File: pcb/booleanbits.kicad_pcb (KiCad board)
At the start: 2 copper layers, 34.3 x 17.8 mm, 3 parts, among them J1 Conn_01x04, J2 Conn_01x04, U1 SN74LVC1G08DBVR

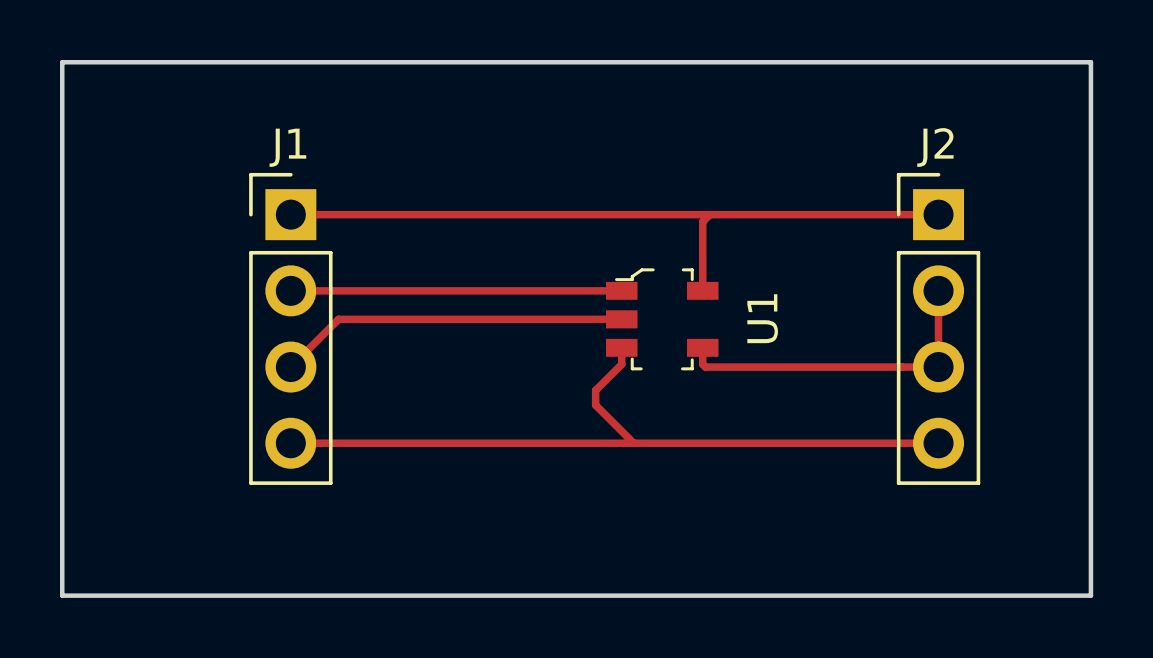
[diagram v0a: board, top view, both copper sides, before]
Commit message: Adding version with better edge footprint. Need bigger traces for my CNC
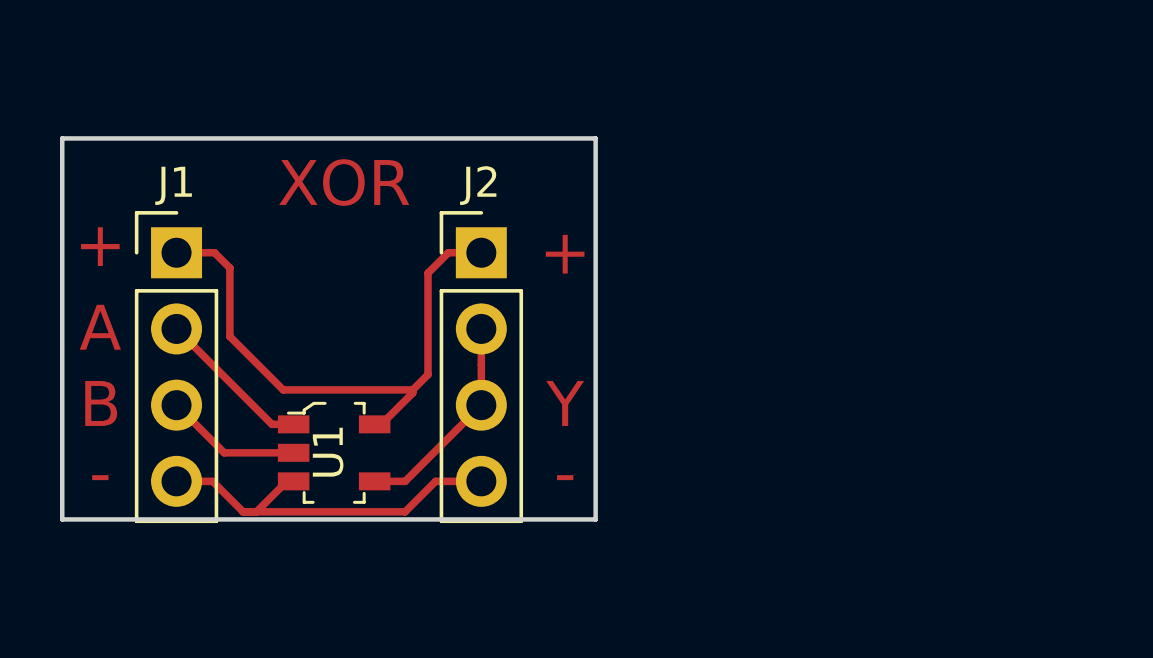
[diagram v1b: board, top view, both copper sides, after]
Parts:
- moved J2 15.3 mm to (35.6, 22.9)
- moved U1 11.8 mm to (30.7, 29.5)
- moved J1 4.02 mm to (25.4, 22.9)
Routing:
- net Net-(J1-Pad4): track 25.7 -> 13.1 mm
- net Net-(J1-Pad3): track 11.7 -> 4.56 mm
- net Net-(J1-Pad2): track 11.0 -> 5.22 mm
- net Net-(J1-Pad1): track 24.2 -> 19.1 mm
- net Net-(J2-Pad2): track 11.0 -> 7.15 mm
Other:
- board size 34.3 x 17.8 mm -> 17.8 x 12.7 mm
- board text added: "+"
- board text added: "-"
- board text added: "A"
- board text added: "B"
- board text added: "XOR"
- board text added: "Y"
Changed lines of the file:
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@@
   (general
     (links 8)
-    (no_connects 8)
-    (area 21.514999 16.434999 55.955001 34.365001)
+    (no_connects 0)
+    (area 20.652381 18.974999 40.30762 37.222857)
     (thickness 1.6)
-    (drawings 4)
-    (tracks 18)
+    (drawings 12)
+    (tracks 28)
     (zones 0)
     (modules 3)
@@
     (pad_to_mask_clearance 0.2)
     (aux_axis_origin 0 0)
-    (visible_elements FFFFEF7F)
+    (grid_origin 21.59 31.75)
+    (visible_elements FFFFFF7F)
     (pcbplotparams
-      (layerselection 0x00030_80000001)
+      (layerselection 0x01080_00000001)
       (usegerberextensions false)
       (excludeedgelayer true)
@@
       (viasonmask false)
       (mode 1)
-      (useauxorigin false)
+      (useauxorigin true)
       (hpglpennumber 1)
       (hpglpenspeed 20)
@@
       (psa4output false)
       (plotreference true)
-      (plotvalue true)
+      (plotvalue false)
       (plotinvisibletext false)
       (padsonsilk false)
@@
       (outputformat 1)
       (mirror false)
-      (drillshape 1)
+      (drillshape 0)
       (scaleselection 1)
-      (outputdirectory /tmp/foo.svg))
+      (outputdirectory plot/))
   )
   (net 0 "")
@@
   )
   (module digikey-footprints:SOT-753 (layer F.Cu)
-    (at 41.59 25.08 270)
-    (fp_text reference U1 (at -0.025 -3.375 270) (layer F.SilkS)
+    (at 30.654 29.53 270)
+    (fp_text reference U1 (at -0.025 0.174 270) (layer F.SilkS)
       (effects (font (size 1 1) (thickness 0.15)))
     )
@@
   )
   (module Pin_Headers:Pin_Header_Straight_1x04_Pitch2.54mm (layer F.Cu)
-    (at 29.21 21.59)
+    (at 25.4 22.86)
     (descr "Through hole straight pin header, 1x04, 2.54mm pitch, single row")
     (tags "Through hole pin header THT 1x04 2.54mm single row")
@@
   )
   (module Pin_Headers:Pin_Header_Straight_1x04_Pitch2.54mm (layer F.Cu)
-    (at 50.8 21.59)
+    (at 35.56 22.86)
     (descr "Through hole straight pin header, 1x04, 2.54mm pitch, single row")
     (tags "Through hole pin header THT 1x04 2.54mm single row")
@@
     )
   )
-  (gr_line (start 55.88 34.29) (end 21.59 34.29) (layer Edge.Cuts) (width 0.15))
-  (gr_line (start 55.88 16.51) (end 55.88 34.29) (layer Edge.Cuts) (width 0.15))
-  (gr_line (start 21.59 16.51) (end 55.88 16.51) (layer Edge.Cuts) (width 0.15))
-  (gr_line (start 21.59 34.29) (end 21.59 16.51) (layer Edge.Cuts) (width 0.15))
-  (segment (start 43.18 21.59) (end 50.8 21.59) (width 0.25) (layer F.Cu) (net 1))
-  (segment (start 29.21 21.59) (end 43.18 21.59) (width 0.25) (layer F.Cu) (net 1))
-  (segment (start 43.18 21.59) (end 42.94 21.83) (width 0.25) (layer F.Cu) (net 1))
-  (segment (start 42.94 21.83) (end 42.94 24.13) (width 0.25) (layer F.Cu) (net 1))
-  (segment (start 50.8 24.13) (end 50.8 26.67) (width 0.25) (layer F.Cu) (net 2))
-  (segment (start 42.94 26.03) (end 42.94 26.58) (width 0.25) (layer F.Cu) (net 2))
-  (segment (start 42.94 26.58) (end 43.03 26.67) (width 0.25) (layer F.Cu) (net 2))
-  (segment (start 43.03 26.67) (end 49.597919 26.67) (width 0.25) (layer F.Cu) (net 2))
-  (segment (start 49.597919 26.67) (end 50.8 26.67) (width 0.25) (layer F.Cu) (net 2))
-  (segment (start 50.8 29.21) (end 40.64 29.21) (width 0.25) (layer F.Cu) (net 3))
-  (segment (start 40.64 29.21) (end 29.21 29.21) (width 0.25) (layer F.Cu) (net 3))
-  (segment (start 39.37 27.45) (end 39.37 27.94) (width 0.25) (layer F.Cu) (net 3))
-  (segment (start 39.37 27.94) (end 40.64 29.21) (width 0.25) (layer F.Cu) (net 3))
-  (segment (start 40.24 26.03) (end 40.24 26.58) (width 0.25) (layer F.Cu) (net 3))
-  (segment (start 40.24 26.58) (end 39.37 27.45) (width 0.25) (layer F.Cu) (net 3))
-  (segment (start 40.24 25.08) (end 30.8 25.08) (width 0.25) (layer F.Cu) (net 4))
-  (segment (start 30.8 25.08) (end 29.21 26.67) (width 0.25) (layer F.Cu) (net 4))
-  (segment (start 29.21 24.13) (end 40.24 24.13) (width 0.25) (layer F.Cu) (net 5))
+  (gr_text XOR (at 30.988 20.574) (layer F.Cu)
+    (effects (font (size 1.5 1.5) (thickness 0.3)))
+  )
+  (gr_text - (at 38.354 30.226) (layer F.Cu)
+    (effects (font (size 1.5 1.5) (thickness 0.3)))
+  )
+  (gr_text + (at 38.354 22.86) (layer F.Cu)
+    (effects (font (size 1.5 1.5) (thickness 0.3)))
+  )
+  (gr_text Y (at 38.354 27.94) (layer F.Cu)
+    (effects (font (size 1.5 1.5) (thickness 0.3)))
+  )
+  (gr_text + (at 22.86 22.606) (layer F.Cu)
+    (effects (font (size 1.5 1.5) (thickness 0.3)))
+  )
+  (gr_text - (at 22.86 30.226) (layer F.Cu)
+    (effects (font (size 1.5 1.5) (thickness 0.3)))
+  )
+  (gr_text B (at 22.86 27.94) (layer F.Cu)
+    (effects (font (size 1.5 1.5) (thickness 0.3)))
+  )
+  (gr_text A (at 22.86 25.4) (layer F.Cu)
+    (effects (font (size 1.5 1.5) (thickness 0.3)))
+  )
+  (gr_line (start 39.37 19.05) (end 21.59 19.05) (layer Edge.Cuts) (width 0.15))
+  (gr_line (start 39.37 31.75) (end 39.37 19.05) (layer Edge.Cuts) (width 0.15))
+  (gr_line (start 21.59 31.75) (end 39.37 31.75) (layer Edge.Cuts) (width 0.15))
+  (gr_line (start 21.59 19.05) (end 21.59 31.75) (layer Edge.Cuts) (width 0.15))
+  (segment (start 25.4 22.86) (end 26.67 22.86) (width 0.25) (layer F.Cu) (net 1))
+  (segment (start 26.67 22.86) (end 27.178 23.368) (width 0.25) (layer F.Cu) (net 1))
+  (segment (start 27.178 23.368) (end 27.178 25.654) (width 0.25) (layer F.Cu) (net 1))
+  (segment (start 27.178 25.654) (end 28.956 27.432) (width 0.25) (layer F.Cu) (net 1))
+  (segment (start 28.956 27.432) (end 33.274 27.432) (width 0.25) (layer F.Cu) (net 1))
+  (segment (start 33.274 27.432) (end 33.274 27.535) (width 0.25) (layer F.Cu) (net 1))
+  (segment (start 33.274 27.535) (end 32.229 28.58) (width 0.25) (layer F.Cu) (net 1))
+  (segment (start 32.229 28.58) (end 32.004 28.58) (width 0.25) (layer F.Cu) (net 1))
+  (segment (start 33.782 23.538) (end 34.46 22.86) (width 0.25) (layer F.Cu) (net 1))
+  (segment (start 33.782 26.924) (end 33.782 23.538) (width 0.25) (layer F.Cu) (net 1))
+  (segment (start 33.274 27.432) (end 33.782 26.924) (width 0.25) (layer F.Cu) (net 1))
+  (segment (start 34.46 22.86) (end 35.56 22.86) (width 0.25) (layer F.Cu) (net 1))
+  (segment (start 35.56 25.4) (end 35.56 26.602081) (width 0.25) (layer F.Cu) (net 2))
+  (segment (start 35.56 26.602081) (end 35.56 27.94) (width 0.25) (layer F.Cu) (net 2))
+  (segment (start 32.004 30.48) (end 33.02 30.48) (width 0.25) (layer F.Cu) (net 2))
+  (segment (start 33.02 30.48) (end 35.56 27.94) (width 0.25) (layer F.Cu) (net 2))
+  (segment (start 27.618081 31.496) (end 28.063 31.496) (width 0.25) (layer F.Cu) (net 3))
+  (segment (start 28.063 31.496) (end 29.079 30.48) (width 0.25) (layer F.Cu) (net 3))
+  (segment (start 29.079 30.48) (end 29.304 30.48) (width 0.25) (layer F.Cu) (net 3))
+  (segment (start 33.02 31.496) (end 34.036 30.48) (width 0.25) (layer F.Cu) (net 3))
+  (segment (start 34.036 30.48) (end 35.56 30.48) (width 0.25) (layer F.Cu) (net 3))
+  (segment (start 27.618081 31.496) (end 33.02 31.496) (width 0.25) (layer F.Cu) (net 3))
+  (segment (start 25.4 30.48) (end 26.602081 30.48) (width 0.25) (layer F.Cu) (net 3))
+  (segment (start 26.602081 30.48) (end 27.618081 31.496) (width 0.25) (layer F.Cu) (net 3))
+  (segment (start 25.4 27.94) (end 26.99 29.53) (width 0.25) (layer F.Cu) (net 4))
+  (segment (start 26.99 29.53) (end 29.304 29.53) (width 0.25) (layer F.Cu) (net 4))
+  (segment (start 25.4 25.4) (end 28.58 28.58) (width 0.25) (layer F.Cu) (net 5))
+  (segment (start 28.58 28.58) (end 29.304 28.58) (width 0.25) (layer F.Cu) (net 5))
   (zone (net 1) (net_name "Net-(J1-Pad1)") (layer F.Cu) (hatch edge 0.508)
     (connect_pads (clearance 0.508))
@@
     (polygon
       (pts
-        (xy 21.59 16.51) (xy 21.59 34.29) (xy 55.88 34.29) (xy 55.88 16.51)
+        (xy 21.59 19.05) (xy 21.59 31.75) (xy 39.37 31.75) (xy 39.37 19.05)
       )
     )
-  )
-  (zone (net 1) (net_name "Net-(J1-Pad1)") (layer F.Cu) (hatch edge 0.508)
-    (connect_pads (clearance 0.508))
-    (min_thickness 0.254)
-    (fill yes (arc_segments 16) (thermal_gap 0.508) (thermal_bridge_width 0.508))
-    (polygon
-      (pts
-        (xy 21.59 16.51) (xy 21.59 34.29) (xy 55.88 34.29) (xy 55.88 16.51)
-      )
-    )
